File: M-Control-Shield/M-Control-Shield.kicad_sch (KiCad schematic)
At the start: 18 parts, among them J1 Conn_01x08, J2 Conn_01x06, J3 Conn_01x10, J4 Conn_01x08

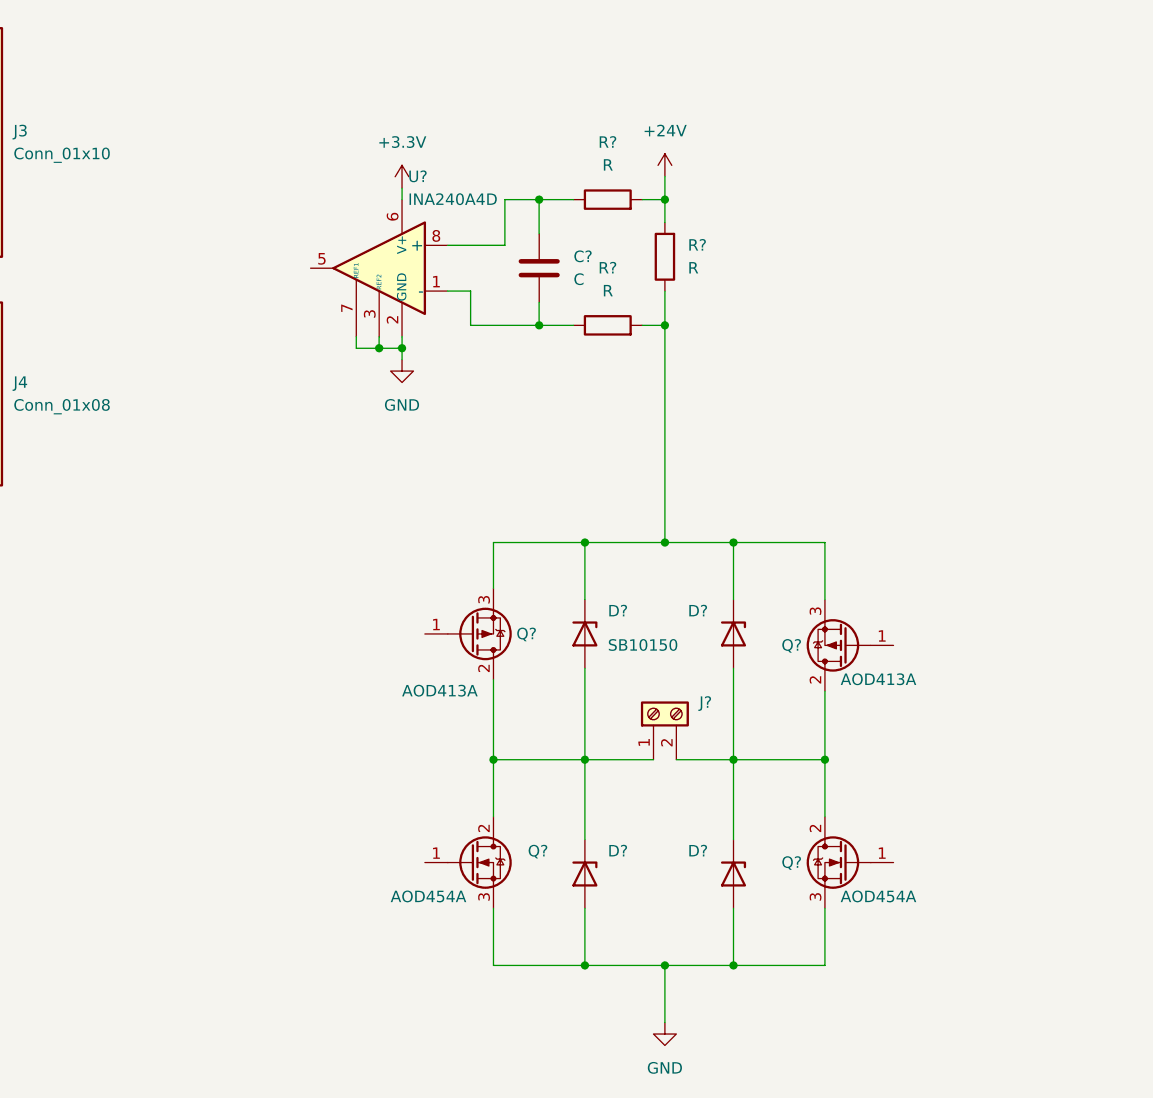
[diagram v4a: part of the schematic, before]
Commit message: Adding MAX17602 gate driver
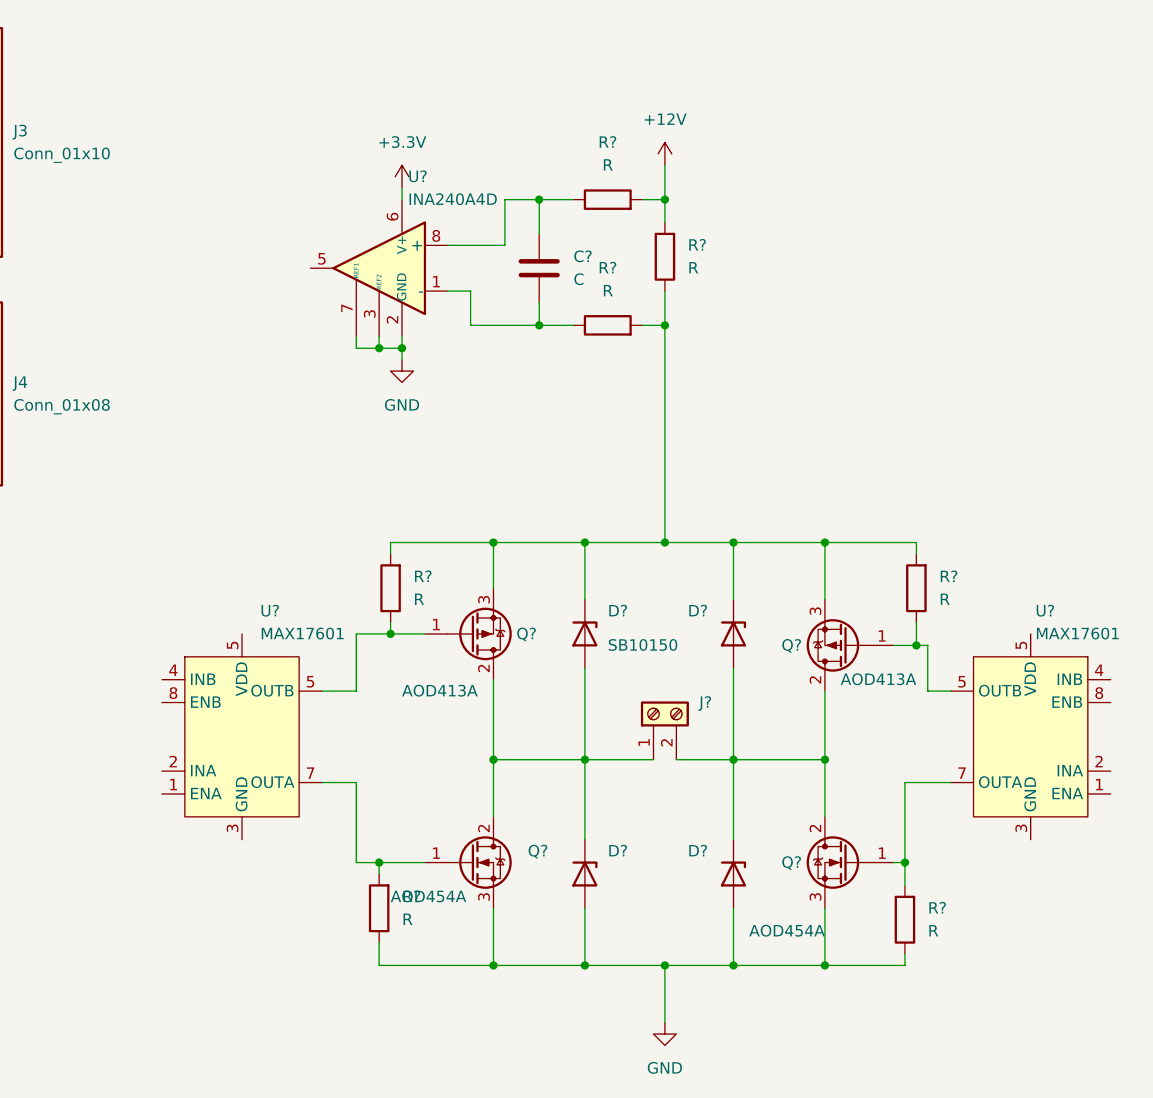
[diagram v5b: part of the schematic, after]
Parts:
- added R? (x4): R, Resistor_SMD:R_0805_2012Metric, symbol Device:R
- added U? (x2): MAX17601, Package_SO:SO-8_3.9x4.9mm_P1.27mm, symbol Gate_Drives:MAX17601
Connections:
- net GND: now also R?.1, R?.1
- net at Q?.1 (G): now also R?.2, U?.7 (OUTA) (x2)
- net at D?.1 (K), D?.1 (K), Q?.3 (S)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: now also R?.2, R?.2
- net at Q?.1 (G): now also R?.1, U?.5 (VDD) (x2)
- net +24V renamed +12V

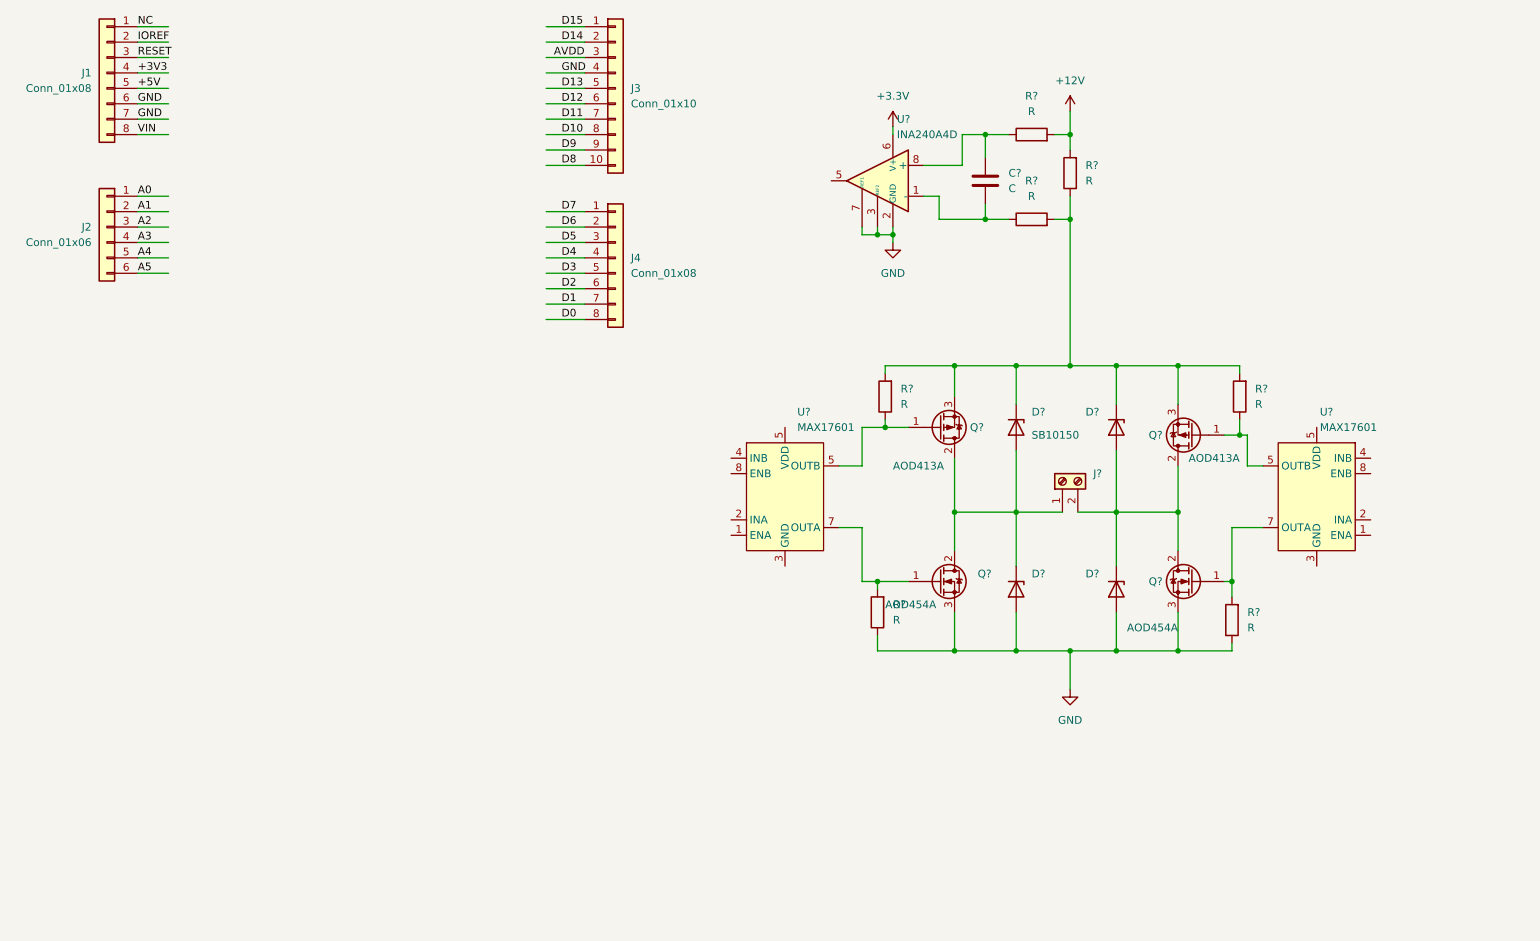
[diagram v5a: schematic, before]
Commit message: Adding cubemx .ioc file for setting up mcu
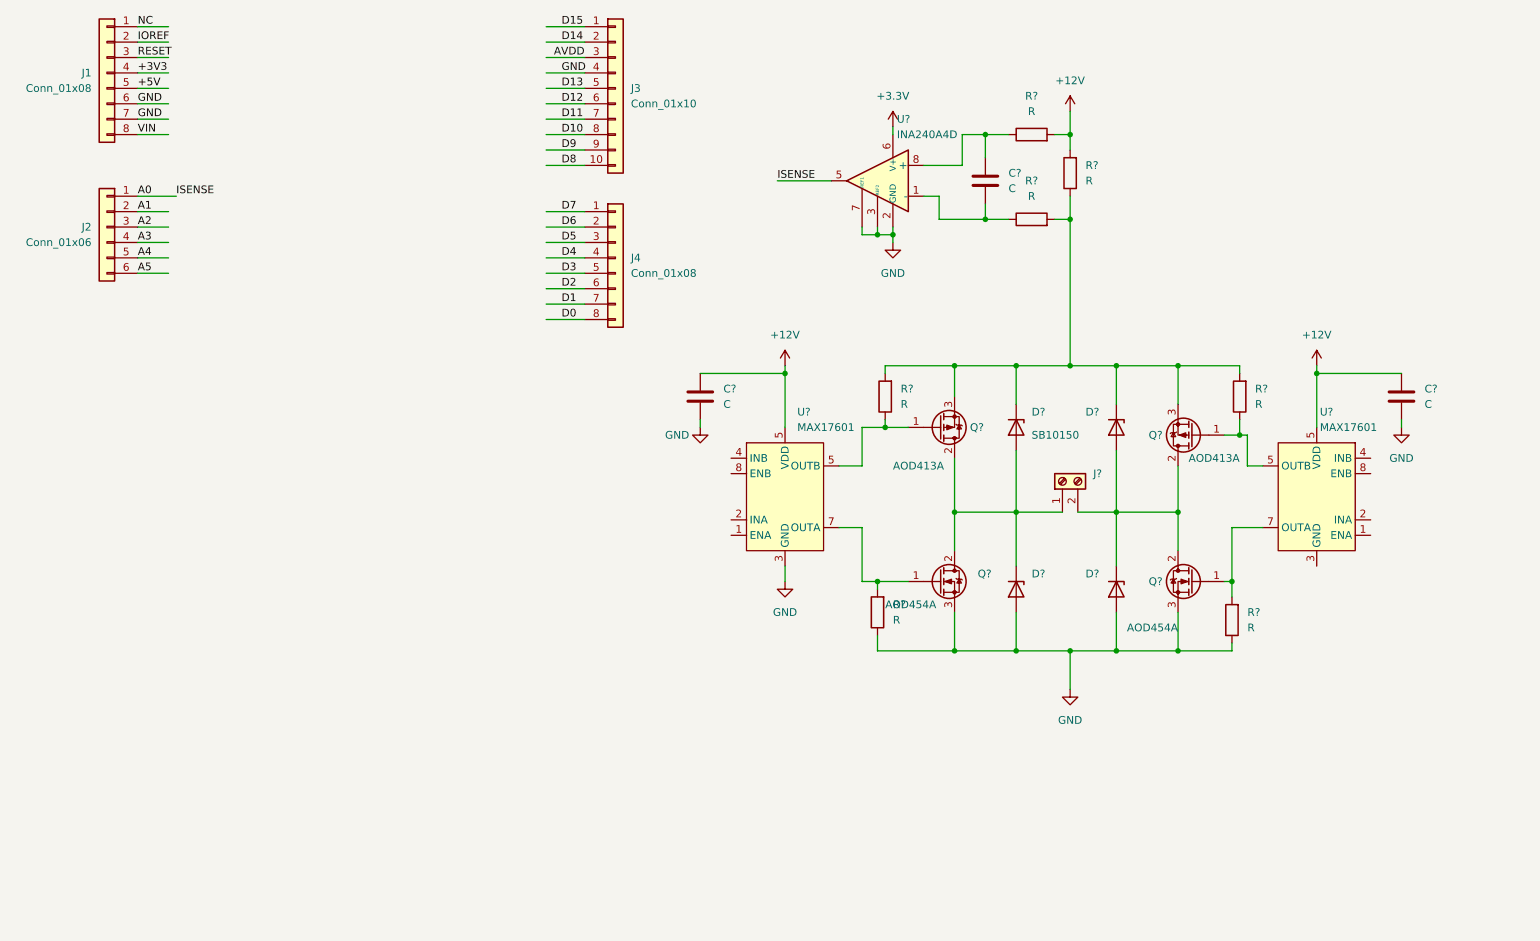
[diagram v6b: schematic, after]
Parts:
- added C? (x2): C, Capacitor_SMD:C_0603_1608Metric, symbol Device:C
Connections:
- net +12V: now also U?.5 (VDD), U?.5 (VDD), C?.1, C?.1
- net A0: now also U?.5
- net GND: now also U?.3 (GND), C?.2, C?.2
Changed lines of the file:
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@@
   (junction (at 228.6 99.06) (diameter 0) (color 0 0 0 0)
   )
+  (junction (at 241.3 88.9) (diameter 0) (color 0 0 0 0)
+  )
   (junction (at 168.91 66.04) (diameter 0) (color 0 0 0 0)
   )
@@
   (junction (at 227.33 123.19) (diameter 0) (color 0 0 0 0)
   )
+  (junction (at 153.67 88.9) (diameter 0) (color 0 0 0 0)
+  )
+  (wire (pts (xy 139.7 88.9) (xy 153.67 88.9))
+    (stroke (width 0) (type default) (color 0 0 0 0))
+  )
   (wire (pts (xy 200.66 49.53) (xy 200.66 52.07))
     (stroke (width 0) (type default) (color 0 0 0 0))
   )
+  (wire (pts (xy 241.3 87.63) (xy 241.3 88.9))
+    (stroke (width 0) (type default) (color 0 0 0 0))
+  )
   (wire (pts (xy 114.3 77.47) (xy 120.65 77.47))
     (stroke (width 0) (type default) (color 0 0 0 0))
@@
     (stroke (width 0) (type default) (color 0 0 0 0))
   )
+  (wire (pts (xy 241.3 88.9) (xy 255.27 88.9))
+    (stroke (width 0) (type default) (color 0 0 0 0))
+  )
+  (wire (pts (xy 153.67 120.65) (xy 153.67 123.19))
+    (stroke (width 0) (type default) (color 0 0 0 0))
+  )
   (wire (pts (xy 114.3 72.39) (xy 120.65 72.39))
     (stroke (width 0) (type default) (color 0 0 0 0))
@@
     (stroke (width 0) (type default) (color 0 0 0 0))
   )
-  (wire (pts (xy 46.99 59.69) (xy 52.07 59.69))
+  (wire (pts (xy 46.99 59.69) (xy 53.34 59.69))
+    (stroke (width 0) (type default) (color 0 0 0 0))
+  )
+  (wire (pts (xy 152.4 57.15) (xy 161.29 57.15))
     (stroke (width 0) (type default) (color 0 0 0 0))
   )
@@
     (stroke (width 0) (type default) (color 0 0 0 0))
   )
+  (wire (pts (xy 139.7 96.52) (xy 139.7 97.79))
+    (stroke (width 0) (type default) (color 0 0 0 0))
+  )
   (wire (pts (xy 218.44 111.76) (xy 218.44 118.11))
     (stroke (width 0) (type default) (color 0 0 0 0))
@@
     (stroke (width 0) (type default) (color 0 0 0 0))
   )
+  (wire (pts (xy 153.67 88.9) (xy 153.67 97.79))
+    (stroke (width 0) (type default) (color 0 0 0 0))
+  )
   (wire (pts (xy 228.6 96.52) (xy 228.6 99.06))
     (stroke (width 0) (type default) (color 0 0 0 0))
@@
     (stroke (width 0) (type default) (color 0 0 0 0))
   )
+  (wire (pts (xy 153.67 87.63) (xy 153.67 88.9))
+    (stroke (width 0) (type default) (color 0 0 0 0))
+  )
+  (wire (pts (xy 241.3 88.9) (xy 241.3 97.79))
+    (stroke (width 0) (type default) (color 0 0 0 0))
+  )
   (wire (pts (xy 114.3 39.37) (xy 120.65 39.37))
     (stroke (width 0) (type default) (color 0 0 0 0))
@@
     (stroke (width 0) (type default) (color 0 0 0 0))
   )
+  (wire (pts (xy 255.27 96.52) (xy 255.27 97.79))
+    (stroke (width 0) (type default) (color 0 0 0 0))
+  )
   (wire (pts (xy 198.12 63.5) (xy 200.66 63.5))
     (stroke (width 0) (type default) (color 0 0 0 0))
@@
     (effects (font (size 1.27 1.27)) (justify left bottom))
   )
+  (label "ISENSE" (at 53.34 59.69 0)
+    (effects (font (size 1.27 1.27)) (justify left bottom))
+  )
   (label "VIN" (at 46.99 49.53 0)
     (effects (font (size 1.27 1.27)) (justify left bottom))
@@
     (effects (font (size 1.27 1.27)) (justify left bottom))
   )
+  (label "ISENSE" (at 152.4 57.15 0)
+    (effects (font (size 1.27 1.27)) (justify left bottom))
+  )
   (label "D6" (at 116.84 64.77 0)
     (effects (font (size 1.27 1.27)) (justify left bottom))
@@
   (label "A1" (at 46.99 62.23 0)
     (effects (font (size 1.27 1.27)) (justify left bottom))
+  )
+  (symbol (lib_id "power:+12V") (at 241.3 87.63 0) (unit 1)
+    (in_bom yes) (on_board yes) (fields_autoplaced)
+    (property "Reference" "#PWR?" (id 0) (at 241.3 91.44 0)
+      (effects (font (size 1.27 1.27)) hide)
+    )
+    (property "Value" "+12V" (id 1) (at 241.3 82.55 0))
+    (property "Footprint" "" (id 2) (at 241.3 87.63 0)
+      (effects (font (size 1.27 1.27)) hide)
+    )
+    (property "Datasheet" "" (id 3) (at 241.3 87.63 0)
+      (effects (font (size 1.27 1.27)) hide)
+    )
+    (pin "1")
   )
   (symbol (lib_id "Connector:Screw_Terminal_01x02") (at 199.39 106.68 90) (unit 1)
@@
     (pin "3")
   )
+  (symbol (lib_id "Device:C") (at 139.7 92.71 0) (unit 1)
+    (in_bom yes) (on_board yes) (fields_autoplaced)
+    (property "Reference" "C?" (id 0) (at 143.51 91.4399 0)
+      (effects (font (size 1.27 1.27)) (justify left))
+    )
+    (property "Value" "C" (id 1) (at 143.51 93.9799 0)
+      (effects (font (size 1.27 1.27)) (justify left))
+    )
+    (property "Footprint" "Capacitor_SMD:C_0603_1608Metric" (id 2) (at 140.6652 96.52 0)
+      (effects (font (size 1.27 1.27)) hide)
+    )
+    (property "Datasheet" "~" (id 3) (at 139.7 92.71 0)
+      (effects (font (size 1.27 1.27)) hide)
+    )
+    (pin "1")
+    (pin "2")
+  )
   (symbol (lib_id "Gate_Drives:MAX17601") (at 241.3 109.22 0) (mirror y) (unit 1)
     (in_bom yes) (on_board yes) (fields_autoplaced)
@@
     (pin "2")
   )
+  (symbol (lib_id "Device:C") (at 255.27 92.71 0) (unit 1)
+    (in_bom yes) (on_board yes) (fields_autoplaced)
+    (property "Reference" "C?" (id 0) (at 259.08 91.4399 0)
+      (effects (font (size 1.27 1.27)) (justify left))
+    )
+    (property "Value" "C" (id 1) (at 259.08 93.9799 0)
+      (effects (font (size 1.27 1.27)) (justify left))
+    )
+    (property "Footprint" "Capacitor_SMD:C_0603_1608Metric" (id 2) (at 256.2352 96.52 0)
+      (effects (font (size 1.27 1.27)) hide)
+    )
+    (property "Datasheet" "~" (id 3) (at 255.27 92.71 0)
+      (effects (font (size 1.27 1.27)) hide)
+    )
+    (pin "1")
+    (pin "2")
+  )
   (symbol (lib_id "Device:R") (at 200.66 55.88 180) (unit 1)
     (in_bom yes) (on_board yes) (fields_autoplaced)
@@
     (pin "6")
   )
+  (symbol (lib_id "power:GND") (at 139.7 97.79 0) (unit 1)
+    (in_bom yes) (on_board yes)
+    (property "Reference" "#PWR?" (id 0) (at 139.7 104.14 0)
+      (effects (font (size 1.27 1.27)) hide)
+    )
+    (property "Value" "GND" (id 1) (at 135.89 99.06 0))
+    (property "Footprint" "" (id 2) (at 139.7 97.79 0)
+      (effects (font (size 1.27 1.27)) hide)
+    )
+    (property "Datasheet" "" (id 3) (at 139.7 97.79 0)
+      (effects (font (size 1.27 1.27)) hide)
+    )
+    (pin "1")
+  )
   (symbol (lib_id "Transistor_FET:SUD50P04-08") (at 179.07 97.79 0) (mirror x) (unit 1)
     (in_bom yes) (on_board yes)
@@
     )
     (property "Datasheet" "" (id 3) (at 200.66 140.97 0)
+      (effects (font (size 1.27 1.27)) hide)
+    )
+    (pin "1")
+  )
+  (symbol (lib_id "power:+12V") (at 153.67 87.63 0) (unit 1)
+    (in_bom yes) (on_board yes) (fields_autoplaced)
+    (property "Reference" "#PWR?" (id 0) (at 153.67 91.44 0)
+      (effects (font (size 1.27 1.27)) hide)
+    )
+    (property "Value" "+12V" (id 1) (at 153.67 82.55 0))
+    (property "Footprint" "" (id 2) (at 153.67 87.63 0)
+      (effects (font (size 1.27 1.27)) hide)
+    )
+    (property "Datasheet" "" (id 3) (at 153.67 87.63 0)
       (effects (font (size 1.27 1.27)) hide)
     )
@@
     (pin "1")
     (pin "2")
+  )
+  (symbol (lib_id "power:GND") (at 255.27 97.79 0) (unit 1)
+    (in_bom yes) (on_board yes) (fields_autoplaced)
+    (property "Reference" "#PWR?" (id 0) (at 255.27 104.14 0)
+      (effects (font (size 1.27 1.27)) hide)
+    )
+    (property "Value" "GND" (id 1) (at 255.27 102.87 0))
+    (property "Footprint" "" (id 2) (at 255.27 97.79 0)
+      (effects (font (size 1.27 1.27)) hide)
+    )
+    (property "Datasheet" "" (id 3) (at 255.27 97.79 0)
+      (effects (font (size 1.27 1.27)) hide)
+    )
+    (pin "1")
+  )
+  (symbol (lib_id "power:GND") (at 153.67 123.19 0) (unit 1)
+    (in_bom yes) (on_board yes) (fields_autoplaced)
+    (property "Reference" "#PWR?" (id 0) (at 153.67 129.54 0)
+      (effects (font (size 1.27 1.27)) hide)
+    )
+    (property "Value" "GND" (id 1) (at 153.67 128.27 0))
+    (property "Footprint" "" (id 2) (at 153.67 123.19 0)
+      (effects (font (size 1.27 1.27)) hide)
+    )
+    (property "Datasheet" "" (id 3) (at 153.67 123.19 0)
+      (effects (font (size 1.27 1.27)) hide)
+    )
+    (pin "1")
   )
   (symbol (lib_id "Connector_Generic:Conn_01x10") (at 125.73 41.91 0) (unit 1)
@@
   )
   (symbol_instances
+    (path "/0c8e124a-56cb-4ad8-bda4-d6c7c3276cac"
+      (reference "#PWR?") (unit 1) (value "+12V") (footprint "")
+    )
     (path "/4fc48f68-a860-487c-be3d-45d1371104c7"
       (reference "#PWR?") (unit 1) (value "+12V") (footprint "")
@@
       (reference "#PWR?") (unit 1) (value "GND") (footprint "")
     )
+    (path "/86fabb81-2449-4bf9-b698-f0a5f3863f7f"
+      (reference "#PWR?") (unit 1) (value "GND") (footprint "")
+    )
     (path "/968c6420-1740-45b5-9560-181657229db0"
       (reference "#PWR?") (unit 1) (value "GND") (footprint "")
     )
+    (path "/a048f788-6f76-4068-a60a-2fc07be998b0"
+      (reference "#PWR?") (unit 1) (value "+12V") (footprint "")
+    )
     (path "/a6551fc8-b101-4d34-9ecf-e2d252afe5f0"
       (reference "#PWR?") (unit 1) (value "+3.3V") (footprint "")
     )
+    (path "/acd96a47-8e90-4264-bacf-886f9c6494b4"
+      (reference "#PWR?") (unit 1) (value "GND") (footprint "")
+    )
+    (path "/bd787270-628c-4213-a2a7-a57f1dbdb500"
+      (reference "#PWR?") (unit 1) (value "GND") (footprint "")
+    )
+    (path "/4791ce53-9d46-4331-bd02-f8ab17111a5c"
+      (reference "C?") (unit 1) (value "C") (footprint "Capacitor_SMD:C_0603_1608Metric")
+    )
+    (path "/71dc759e-b3d3-4ec5-b1db-ec8646878b07"
+      (reference "C?") (unit 1) (value "C") (footprint "Capacitor_SMD:C_0603_1608Metric")
+    )
     (path "/a2e75628-4124-406a-8351-4d2fbe7eec11"
